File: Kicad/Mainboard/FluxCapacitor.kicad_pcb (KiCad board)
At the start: 2 copper layers, 100 x 100 mm, 101 parts, among them J1 PJ-002A, J2 TM_1, J3 TM_2, J7 TM_4, J8 TM_2, J9 RELAY, M1 SYS_FAN, Q2 IRF4905PBF, Q3 2N7000, Q4 2N7000, U1 OKI-78SR-5_1.5-W36-C, U2 ESP32_DEVBOARD, U4 HT16K33_DEVBOARD, U5 PCA9306DCUR

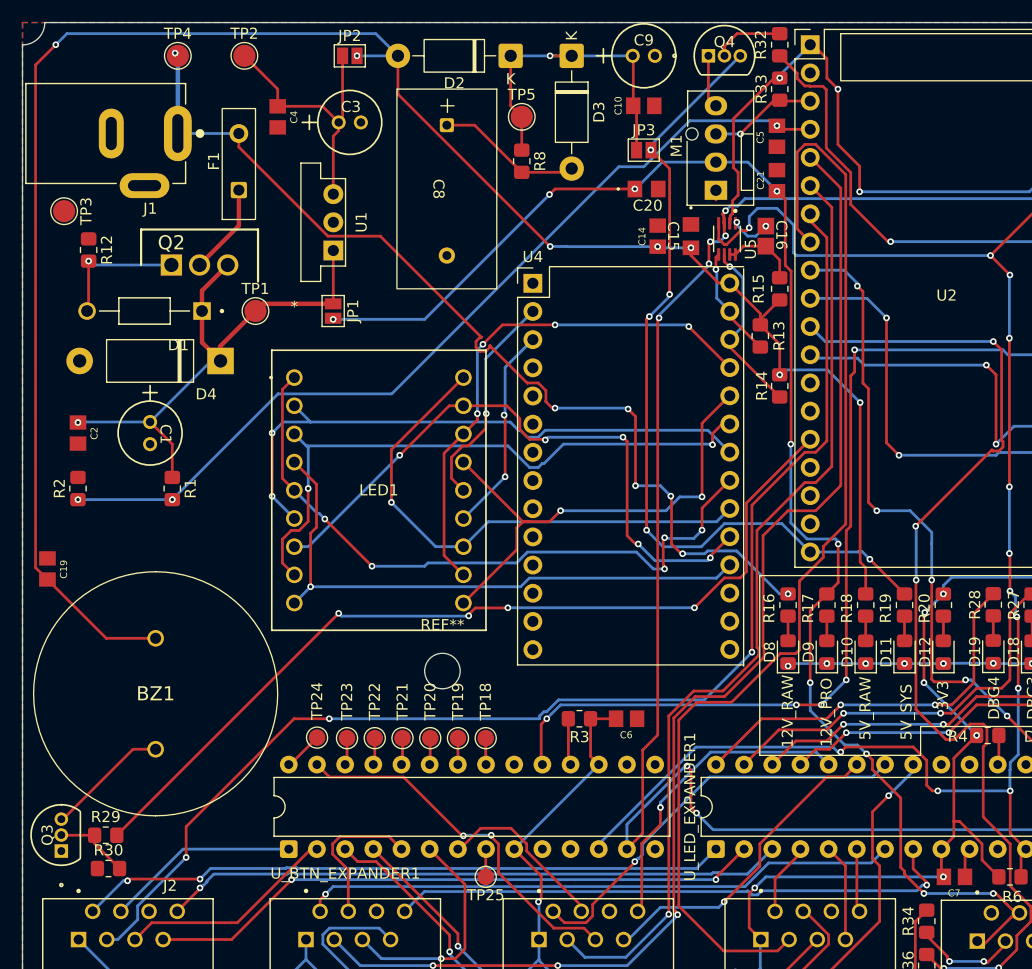
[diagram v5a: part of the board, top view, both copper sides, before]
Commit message: Finished project
Made daughterboard pcbs, fixed silkscreen errors on mainboard pcb, generated GERBERs and drill files
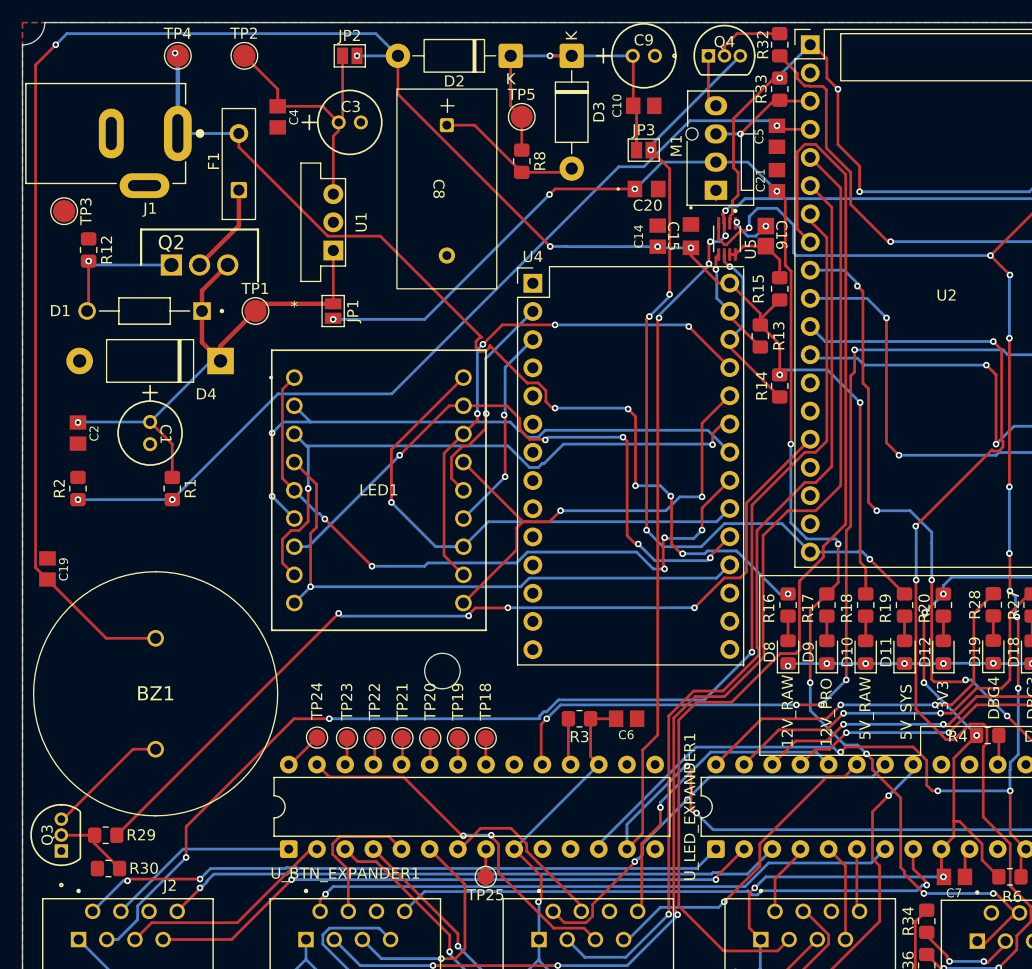
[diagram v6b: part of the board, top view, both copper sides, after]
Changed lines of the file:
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@@
 		(filling no)
 		(pcbplotparams
-			(layerselection 0x00000000_00000000_55555555_5755f5ff)
+			(layerselection 0x00000000_00000000_55555555_575555ff)
 			(plot_on_all_layers_selection 0x00000000_00000000_00000000_00000000)
 			(disableapertmacros no)
@@
 			(outputformat 1)
 			(mirror no)
-			(drillshape 1)
+			(drillshape 0)
 			(scaleselection 1)
-			(outputdirectory "C:/Users/1283a/Downloads/")
+			(outputdirectory "../Gerbers/Mainboard/")
 		)
 	)
@@
 			(effects
 				(font
-					(size 0.630261 0.630261)
+					(size 0.8 0.8)
 					(thickness 0.15)
 				)
@@
 			)
 		)
-		(property "Description" "Unpolarized ceramic capacitor"
+		(property "Description" ""
 			(at 0 0 270)
 			(layer "F.Fab")
@@
 		(sheetname "/")
 		(sheetfile "FluxCapacitor.kicad_sch")
-		(units
-			(unit
-				(name "A")
-				(pins "1" "2")
-			)
-		)
 		(attr smd)
 		(duplicate_pad_numbers_are_jumpers no)
@@
 		(tags "resistor handsolder")
 		(property "Reference" "R29"
-			(at 0 -1.65 0)
+			(at 3.2 0 0)
 			(layer "F.SilkS")
 			(effects
@@
 		(sheetname "/")
 		(sheetfile "FluxCapacitor.kicad_sch")
-		(units
-			(unit
-				(name "A")
-				(pins "1" "2")
-			)
-		)
 		(attr smd)
 		(duplicate_pad_numbers_are_jumpers no)
@@
 		(tags "resistor handsolder")
 		(property "Reference" "R32"
-			(at 0 1.7 90)
+			(at 0 1.5 90)
 			(layer "F.SilkS")
 			(effects
@@
 		(descr "<b>CAPACITOR</b><p>")
 		(property "Reference" "C6"
-			(at 0.03002 -1.470796 0)
+			(at 0.03002 -1.470796 180)
 			(layer "F.SilkS")
 			(effects
 				(font
-					(size 0.630261 0.630261)
+					(size 0.8 0.8)
 					(thickness 0.15)
 				)
@@
 		)
 		(property "Value" "0.1UF"
-			(at 2.430305 1.540191 0)
+			(at 2.430305 1.540191 180)
 			(layer "F.Fab")
 			(effects
@@
 		)
 		(property "Datasheet" ""
-			(at 0 0 0)
+			(at 0 0 180)
 			(layer "F.Fab")
 			(hide yes)
@@
 			)
 		)
-		(property "Description" "Unpolarized ceramic capacitor"
-			(at 0 0 0)
+		(property "Description" ""
+			(at 0 0 180)
 			(layer "F.Fab")
 			(hide yes)
@@
 		(sheetname "/")
 		(sheetfile "FluxCapacitor.kicad_sch")
-		(units
-			(unit
-				(name "A")
-				(pins "1" "2")
-			)
-		)
 		(attr smd)
 		(duplicate_pad_numbers_are_jumpers no)
@@
 		(tags "resistor handsolder")
 		(property "Reference" "R30"
-			(at 0 -1.65 0)
+			(at 3.2 0 0)
 			(layer "F.SilkS")
 			(effects
@@
 		(sheetname "/")
 		(sheetfile "FluxCapacitor.kicad_sch")
-		(units
-			(unit
-				(name "A")
-				(pins "1" "2")
-			)
-		)
 		(attr smd)
 		(duplicate_pad_numbers_are_jumpers no)
@@
 			(at 0 -4.15 0)
 			(layer "F.SilkS")
+			(hide yes)
 			(effects
 				(font
@@
 			(at 0 4.15 0)
 			(layer "F.Fab")
+			(hide yes)
 			(effects
 				(font
@@
 		(at 102.75 70.75 180)
 		(property "Reference" "D1"
-			(at -3.05 -3.0725 180)
+			(at 7.6 0 180)
 			(layer "F.SilkS")
 			(effects
@@
 		(sheetname "/")
 		(sheetfile "FluxCapacitor.kicad_sch")
-		(units
-			(unit
-				(name "A")
-				(pins "2" "1")
-			)
-		)
 		(attr through_hole)
 		(duplicate_pad_numbers_are_jumpers no)
@@
 		(descr "<b>CAPACITOR</b><p>")
 		(property "Reference" "C14"
-			(at 0.03002 1.4 90)
+			(at 0.03002 1.7 270)
 			(layer "F.SilkS")
 			(effects
 				(font
-					(size 0.630261 0.630261)
+					(size 0.8 0.8)
 					(thickness 0.15)
 				)
@@
 		)
 		(property "Value" "0.1UF"
-			(at 2.430305 1.540191 90)
+			(at 2.430305 1.540191 270)
 			(layer "F.Fab")
 			(effects
@@
 		)
 		(property "Datasheet" ""
-			(at 0 0 90)
+			(at 0 0 270)
 			(layer "F.Fab")
 			(hide yes)
@@
 			)
 		)
-		(property "Description" "Unpolarized capacitor"
-			(at 0 0 90)
+		(property "Description" ""
+			(at 0 0 270)
 			(layer "F.Fab")
 			(hide yes)
@@
 		(descr "<b>CAPACITOR</b><p>")
 		(property "Reference" "C19"
-			(at 0.03002 -1.470796 90)
+			(at 0.03002 -1.470796 270)
 			(layer "F.SilkS")
 			(effects
 				(font
-					(size 0.630261 0.630261)
+					(size 0.8 0.8)
 					(thickness 0.15)
 				)
@@
 		)
 		(property "Value" "0.1UF"
-			(at 2.430305 1.540191 90)
+			(at 2.430305 1.540191 270)
 			(layer "F.Fab")
 			(effects
@@
 		)
 		(property "Datasheet" ""
-			(at 0 0 90)
+			(at 0 0 270)
 			(layer "F.Fab")
 			(hide yes)
@@
 			)
 		)
-		(property "Description" "Unpolarized capacitor"
-			(at 0 0 90)
+		(property "Description" ""
+			(at 0 0 270)
 			(layer "F.Fab")
 			(hide yes)
@@
 		(sheetname "/")
 		(sheetfile "FluxCapacitor.kicad_sch")
-		(units
-			(unit
-				(name "A")
-				(pins "1" "2")
-			)
-		)
 		(attr smd)
 		(duplicate_pad_numbers_are_jumpers no)
@@
 		(tags "Diode DO-41_SOD81 series Axial Horizontal pin pitch 10.16mm  length 5.2mm diameter 2.7mm")
 		(property "Reference" "D2"
-			(at 5.08 -2.47 180)
+			(at 5.08 -2.3 180)
 			(layer "F.SilkS")
 			(effects
@@
 		(sheetname "/")
 		(sheetfile "FluxCapacitor.kicad_sch")
-		(units
-			(unit
-				(name "A")
-				(pins "1" "2")
-			)
-		)
 		(attr through_hole)
 		(duplicate_pad_numbers_are_jumpers no)
@@
 			(effects
 				(font
-					(size 0.630261 0.630261)
+					(size 0.8 0.8)
 					(thickness 0.15)
 				)
@@
 			)
 		)
-		(property "Description" "Unpolarized ceramic capacitor"
+		(property "Description" ""
 			(at 0 0 270)
 			(layer "F.Fab")
@@
 		(sheetname "/")
 		(sheetfile "FluxCapacitor.kicad_sch")
-		(units
-			(unit
-				(name "A")
-				(pins "1" "2")
-			)
-		)
 		(attr smd)
 		(duplicate_pad_numbers_are_jumpers no)
@@
 		(descr "<b>CAPACITOR</b><p>")
 		(property "Reference" "C5"
-			(at 0.1 1.5 90)
+			(at 0 1.6 270)
 			(layer "F.SilkS")
 			(effects
 				(font
-					(size 0.630261 0.630261)
+					(size 0.8 0.8)
 					(thickness 0.15)
 				)
@@
 		)
 		(property "Value" "0.1UF"
-			(at 2.430305 1.540191 90)
+			(at 2.430305 1.540191 270)
 			(layer "F.Fab")
 			(effects
@@
 		)
 		(property "Datasheet" ""
-			(at 0 0 90)
+			(at 0 0 270)
 			(layer "F.Fab")
 			(hide yes)
@@
 			)
 		)
-		(property "Description" "Unpolarized ceramic capacitor"
-			(at 0 0 90)
+		(property "Description" ""
+			(at 0 0 270)
 			(layer "F.Fab")
 			(hide yes)
@@
 		(descr "<b>CAPACITOR</b><p>")
 		(property "Reference" "C10"
-			(at -2.3 0 90)
+			(at -2.4 0 90)
 			(layer "F.SilkS")
 			(effects
 				(font
-					(size 0.630261 0.630261)
+					(size 0.8 0.8)
 					(thickness 0.15)
 				)
@@
 			)
 		)
-		(property "Description" "Unpolarized capacitor"
+		(property "Description" ""
 			(at 0 0 0)
 			(layer "F.Fab")
@@
 			(effects
 				(font
-					(size 0.630261 0.630261)
+					(size 0.8 0.8)
 					(thickness 0.15)
 				)
@@
 		(sheetname "/")
 		(sheetfile "FluxCapacitor.kicad_sch")
-		(units
-			(unit
-				(name "A")
-				(pins "1" "2")
-			)
-		)
 		(attr smd dnp)
 		(duplicate_pad_numbers_are_jumpers no)
@@
 		(descr "<b>CAPACITOR</b><p>")
 		(property "Reference" "C7"
-			(at 0.03002 -1.470796 0)
+			(at 0.03002 -1.470796 180)
 			(layer "F.SilkS")
 			(effects
 				(font
-					(size 0.630261 0.630261)
+					(size 0.8 0.8)
 					(thickness 0.15)
 				)
@@
 		)
 		(property "Value" "0.1UF"
-			(at 2.430305 1.540191 0)
+			(at 2.430305 1.540191 180)
 			(layer "F.Fab")
 			(effects
@@
 		)
 		(property "Datasheet" ""
-			(at 0 0 0)
+			(at 0 0 180)
 			(layer "F.Fab")
 			(hide yes)
@@
 			)
 		)
-		(property "Description" "Unpolarized ceramic capacitor"
-			(at 0 0 0)
+		(property "Description" ""
+			(at 0 0 180)
 			(layer "F.Fab")
 			(hide yes)
@@
 		(sheetname "/")
 		(sheetfile "FluxCapacitor.kicad_sch")
-		(units
-			(unit
-				(name "A")
-				(pins "1" "2")
-			)
-		)
 		(attr smd)
 		(duplicate_pad_numbers_are_jumpers no)
